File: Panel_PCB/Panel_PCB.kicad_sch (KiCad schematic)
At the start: 98 parts, among them J1 DC, J10 Relay 3, J11 Relay 4, J12 Terminal A, J13 Terminal B, J2 Bateria, J3 Sensor IN, J4 Sensor OUT, J5 Boton 1, J6 Boton 2, J7 Boton 3, J8 Relay 1, J9 Relay 2, K1 SANYOU_SRD_Form_C, K2 SANYOU_SRD_Form_C, K3 SANYOU_SRD_Form_C, K4 SANYOU_SRD_Form_C, K5 EC2-4.5SNU, K7 SANYOU_SRD_Form_C, Q1 2N2222A, Q2 2N2222A, Q3 2N2222A, Q4 2N2222A, Q7 2N2222A, U1 TLP291, U10 LM1117T-3.3, U11 LM7812_TO220, U12 DS1307+, U13 LM311, U2 TLP291, U3 TLP291, U4 TLP291, U5 LM7805_TO220, U6 LM1117T-3.3, U7 LM7805_TO220, U8 LM7805_TO220, U9 LM1117T-3.3, Y1 Crystal

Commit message: Actualización
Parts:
- removed C15: 0.1 μF, Capacitor_THT:C_Disc_D3.0mm_W1.6mm_P2.50mm, symbol Device:C_US
- removed C16: 0.22 μF, Capacitor_THT:C_Disc_D3.0mm_W1.6mm_P2.50mm, symbol Device:C_US
- removed D10, D11, D15, D17, D8: 1N4001, Diode_THT:D_DO-41_SOD81_P10.16mm_Horizontal, symbol Diode:1N4001
- removed R15, R16: 100 Ω 2W, Resistor_THT:R_Axial_DIN0617_L17.0mm_D6.0mm_P25.40mm_Horizontal, symbol Device:R_US
- removed R17: 1K, Resistor_THT:R_Axial_DIN0309_L9.0mm_D3.2mm_P12.70mm_Horizontal, symbol Device:R_US
- removed U11: LM7812_TO220, Package_TO_SOT_THT:TO-220-3_Vertical, symbol Regulator_Linear:LM7812_TO220
- added D19: 1N4001, Diode_THT:D_DO-41_SOD81_P10.16mm_Horizontal, symbol Diode:1N4001
- R2: value 100 Ω 2W -> 20 Ω 10W
- R21: value 220 -> 50
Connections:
- net at C1.2, C10.2, C11.2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: now also J1.1 (Pin_1), D19.2 (A)
- net at D16.1 (K), K7.5: now also D1.1 (K), K5.1, K5.4, D19.1 (K)
- net at J2.1 (Pin_1): now also D18.2 (A), K5.10, K7.3; no longer D7.2 (A)
- net at K5.5, R2.1: now also D7.1 (K); no longer K5.9
- net at D1.2 (A), F1.2: now also K7.1
- new net: D7.2 (A), K5.9
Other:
- note added: "El circuito puede funcionar a 10 VDC y 1 A debido a esto y por simplicidad, se decide cargar la bateria con 12 VDC"
- note removed: "Se necesitan al menos 14 VDC"
- moved on the sheet: D1, D7, K5

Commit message: Actualización
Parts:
- removed R2: 20 Ω 10W, Resistor_THT:R_Axial_DIN0617_L17.0mm_D6.0mm_P25.40mm_Horizontal, symbol Device:R_US
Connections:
- net at D7.1 (K), K5.5: now also C2.1, C7.1, C9.1, D2.1 (K), D3.1 (K), D4.1 (K), D5.1 (K), D6.1 (K), D9.2 (A), K1.5, K2.5, K3.5, K4.5, R10.1, R4.1, R6.1, R8.1, U7.1 (VI), U8.1 (VI)
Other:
- note added: "Con base en pruebas, aqui hay 11 VDC"
- note removed: "Debido a los diodos anteriores se debe virificar si hay 12V exactos"
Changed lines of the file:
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@@
 		)
 	)
-	(text "Debido a los diodos anteriores \nse debe virificar si hay 12V exactos"
+	(text "Con base en pruebas, aqui hay 11 VDC"
 		(exclude_from_sim no)
-		(at 309.626 236.982 0)
+		(at 309.88 244.602 0)
 		(effects
 			(font
@@
 	)
 	(junction
+		(at 300.99 247.65)
+		(diameter 0)
+		(color 0 0 0 0)
+	)
+	(junction
 		(at 482.6 73.66)
 		(diameter 0)
@@
 	)
 	(junction
-		(at 300.99 247.65)
-		(diameter 0)
-		(color 0 0 0 0)
-	)
-	(junction
 		(at 468.63 193.04)
 		(diameter 0)
@@
 	(wire
 		(pts
+			(xy 288.29 247.65) (xy 300.99 247.65)
+		)
+		(stroke
+			(width 0)
+			(type default)
+			(color 255 0 0 1)
+		)
+	)
+	(wire
+		(pts
 			(xy 224.79 182.88) (xy 224.79 200.66)
 		)
@@
 	(wire
 		(pts
-			(xy 288.29 247.65) (xy 292.1 247.65)
-		)
-		(stroke
-			(width 0)
-			(type default)
-			(color 255 0 0 1)
-		)
-	)
-	(wire
-		(pts
 			(xy 482.6 50.8) (xy 482.6 58.42)
 		)
@@
 	(wire
 		(pts
-			(xy 299.72 247.65) (xy 300.99 247.65)
-		)
-		(stroke
-			(width 0)
-			(type default)
-			(color 255 0 0 1)
-		)
-	)
-	(wire
-		(pts
 			(xy 203.2 194.31) (xy 203.2 204.47)
 		)
@@
 					(unit 1)
 				)
-			)
-		)
-	)
-	(symbol
-		(lib_id "Device:R_US")
-		(at 295.91 247.65 90)
-		(unit 1)
-		(exclude_from_sim no)
-		(in_bom yes)
-		(on_board yes)
-		(dnp no)
-		(fields_autoplaced yes)
-		(property "Reference" "R2"
-			(at 295.91 241.3 90)
-			(effects
-				(font
-					(size 1.27 1.27)
-				)
-			)
-		)
-		(property "Value" "20 Ω 10W"
-			(at 295.91 243.84 90)
-			(effects
-				(font
-					(size 1.27 1.27)
-				)
-			)
-		)
-		(property "Footprint" "Resistor_THT:R_Axial_DIN0617_L17.0mm_D6.0mm_P25.40mm_Horizontal"
-			(at 296.164 246.634 90)
-			(effects
-				(font
-					(size 1.27 1.27)
-				)
-				(hide yes)
-			)
-		)
-		(property "Datasheet" "~"
-			(at 295.91 247.65 0)
-			(effects
-				(font
-					(size 1.27 1.27)
-				)
-				(hide yes)
-			)
-		)
-		(property "Description" "Resistor, US symbol"
-			(at 295.91 247.65 0)
-			(effects
-				(font
-					(size 1.27 1.27)
-				)
-				(hide yes)
-			)
-		)
-		(pin "2"
-		)
-		(pin "1"
-		)
-		(instances
-			(project "Panel_PCB"
-				(path "/f7146f60-4eeb-4a38-9050-767b0cc7f13c"
-					(reference "R2")
-					(unit 1)
-				)

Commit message: Actualización
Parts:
- removed D9: 1N4001, Diode_THT:D_DO-41_SOD81_P10.16mm_Horizontal, symbol Diode:1N4001
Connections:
- net at D12.2 (A): now also C2.1, C7.1, C9.1, D2.1 (K), D3.1 (K), D4.1 (K), D5.1 (K), D6.1 (K), D7.1 (K), K1.5, K2.5, K3.5, K4.5, K5.5, R10.1, R4.1, R6.1, R8.1, U7.1 (VI), U8.1 (VI)
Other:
- note added: "AUX"
- note added: "Puerta"
- note removed: "Puerta 1"
- note removed: "Puerta 2"
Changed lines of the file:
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@@
 		)
 	)
-	(text "Puerta 2"
+	(text "Luz emergencia"
 		(exclude_from_sim no)
 		(at 488.95 483.362 0)
@@
 		)
 	)
-	(text "Puerta 1"
+	(text "Puerta"
 		(exclude_from_sim no)
 		(at 416.306 484.124 0)
@@
 		)
 	)
-	(text "Luz emergencia"
+	(text "Señal panico"
 		(exclude_from_sim no)
 		(at 560.578 483.108 0)
@@
 		)
 	)
-	(text "Señal panico"
+	(text "AUX\n"
 		(exclude_from_sim no)
 		(at 634.746 482.854 0)
@@
 	(wire
 		(pts
+			(xy 356.87 53.34) (xy 356.87 247.65)
+		)
+		(stroke
+			(width 0)
+			(type default)
+			(color 255 0 0 1)
+		)
+	)
+	(wire
+		(pts
 			(xy 542.29 339.09) (xy 471.17 339.09)
 		)
@@
 	(wire
 		(pts
-			(xy 356.87 53.34) (xy 356.87 54.61)
-		)
-		(stroke
-			(width 0)
-			(type default)
-		)
-	)
-	(wire
-		(pts
 			(xy 469.9 215.9) (xy 565.15 215.9)
 		)
@@
 	(wire
 		(pts
-			(xy 356.87 62.23) (xy 356.87 247.65)
-		)
-		(stroke
-			(width 0)
-			(type default)
-			(color 255 0 0 1)
-		)
-	)
-	(wire
-		(pts
 			(xy 148.59 247.65) (xy 154.94 247.65)
 		)
@@
 					(unit 1)
 				)
-			)
-		)
-	)
-	(symbol
-		(lib_id "Diode:1N4001")
-		(at 356.87 58.42 270)
-		(unit 1)
-		(exclude_from_sim no)
-		(in_bom yes)
-		(on_board yes)
-		(dnp no)
-		(property "Reference" "D9"
-			(at 360.426 57.404 0)
-			(effects
-				(font
-					(size 1.27 1.27)
-				)
-				(justify left)
-			)
-		)
-		(property "Value" "1N4001"
-			(at 362.712 55.118 0)
-			(effects
-				(font
-					(size 1.27 1.27)
-				)
-				(justify left)
-			)
-		)
-		(property "Footprint" "Diode_THT:D_DO-41_SOD81_P10.16mm_Horizontal"
-			(at 356.87 58.42 0)
-			(effects
-				(font
-					(size 1.27 1.27)
-				)
-				(hide yes)
-			)
-		)
-		(property "Datasheet" "http://www.vishay.com/docs/88503/1n4001.pdf"
-			(at 356.87 58.42 0)
-			(effects
-				(font
-					(size 1.27 1.27)
-				)
-				(hide yes)
-			)
-		)
-		(property "Description" "50V 1A General Purpose Rectifier Diode, DO-41"
-			(at 356.87 58.42 0)
-			(effects
-				(font
-					(size 1.27 1.27)
-				)
-				(hide yes)
-			)
-		)
-		(property "Sim.Device" "D"
-			(at 356.87 58.42 0)
-			(effects
-				(font
-					(size 1.27 1.27)
-				)
-				(hide yes)
-			)
-		)
-		(property "Sim.Pins" "1=K 2=A"
-			(at 356.87 58.42 0)
-			(effects
-				(font
-					(size 1.27 1.27)
-				)
-				(hide yes)
-			)
-		)
-		(pin "1"
-		)
-		(pin "2"
-		)
-		(instances
-			(project "Panel_PCB"
-				(path "/f7146f60-4eeb-4a38-9050-767b0cc7f13c"
-					(reference "D9")
-					(unit 1)
-				)

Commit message: Actualización del esquema y el software
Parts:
- added J14: Boton D (4), TerminalBlock_Phoenix:TerminalBlock_Phoenix_MKDS-1,5-2-5.08_1x02_P5.08mm_Horizontal, symbol Connector:Screw_Terminal_01x02
- J5: value Boton 1 -> Boton A (1)
- J6: value Boton 2 -> Boton B (2)
- J7: value Boton 3 -> Boton C (3)
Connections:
- net at C1.2, C10.2, C11.2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: now also J14.1 (Pin_1)
- net at J13.13 (Pin_13): now also J14.2 (Pin_2)
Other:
- note added: "Boton A (1)"
- note added: "Boton B (2)"
- note added: "Boton C (3)"
- note added: "Boton D (4)"
- note removed: "Boton 1"
- note removed: "Boton 2"
- note removed: "Boton 3"
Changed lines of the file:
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@@
 		)
 	)
-	(text "Boton 1"
+	(text "Boton A (1)"
 		(exclude_from_sim no)
-		(at 596.138 178.562 0)
+		(at 601.726 178.562 0)
 		(effects
 			(font
@@
 		)
 	)
-	(text "Boton 2"
+	(text "Boton B (2)"
 		(exclude_from_sim no)
 		(at 596.392 202.946 0)
@@
 		)
 	)
-	(text "Boton 3"
+	(text "Boton C (3)"
 		(exclude_from_sim no)
 		(at 595.122 227.33 0)
@@
 		)
 	)
+	(text "Boton D (4)"
+		(exclude_from_sim no)
+		(at 591.82 250.444 0)
+		(effects
+			(font
+				(size 1.27 1.27)
+			)
+		)
+	)
 	(text "Sensor salida"
 		(exclude_from_sim no)
@@
 	)
 	(junction
-		(at 535.94 129.54)
-		(diameter 0)
-		(color 0 0 0 0)
-	)
-	(junction
 		(at 411.48 154.94)
 		(diameter 0)
@@
 	)
 	(junction
+		(at 528.32 193.04)
+		(diameter 0)
+		(color 0 0 0 0)
+	)
+	(junction
 		(at 308.61 267.97)
 		(diameter 0)
@@
 	)
 	(junction
+		(at 478.79 129.54)
+		(diameter 0)
+		(color 0 0 0 0)
+	)
+	(junction
 		(at 433.07 193.04)
 		(diameter 0)
@@
 	)
 	(junction
+		(at 478.79 154.94)
+		(diameter 0)
+		(color 0 0 0 0)
+	)
+	(junction
 		(at 687.07 311.15)
 		(diameter 0)
@@
 	)
 	(junction
-		(at 535.94 154.94)
-		(diameter 0)
-		(color 0 0 0 0)
-	)
-	(junction
 		(at 468.63 177.8)
 		(diameter 0)
@@
 	(wire
 		(pts
+			(xy 478.79 129.54) (xy 613.41 129.54)
+		)
+		(stroke
+			(width 0)
+			(type default)
+		)
+	)
+	(wire
+		(pts
 			(xy 154.94 167.64) (xy 154.94 247.65)
 		)
@@
 	(wire
 		(pts
-			(xy 435.61 154.94) (xy 535.94 154.94)
+			(xy 435.61 154.94) (xy 478.79 154.94)
 		)
 		(stroke
@@
 	(wire
 		(pts
+			(xy 548.64 193.04) (xy 528.32 193.04)
+		)
+		(stroke
+			(width 0)
+			(type default)
+			(color 0 0 0 1)
+		)
+	)
+	(wire
+		(pts
 			(xy 542.29 265.43) (xy 698.5 265.43)
 		)
@@
 	(wire
 		(pts
+			(xy 478.79 154.94) (xy 610.87 154.94)
+		)
+		(stroke
+			(width 0)
+			(type default)
+		)
+	)
+	(wire
+		(pts
 			(xy 441.96 189.23) (xy 441.96 193.04)
 		)
@@
 	(wire
 		(pts
+			(xy 596.9 270.51) (xy 532.13 270.51)
+		)
+		(stroke
+			(width 0)
+			(type default)
+		)
+	)
+	(wire
+		(pts
 			(xy 534.67 408.94) (xy 537.21 408.94)
 		)
@@
 	(wire
 		(pts
-			(xy 414.02 129.54) (xy 535.94 129.54)
+			(xy 414.02 129.54) (xy 478.79 129.54)
 		)
 		(stroke
@@
 	(wire
 		(pts
-			(xy 468.63 177.8) (xy 535.94 177.8)
+			(xy 468.63 177.8) (xy 478.79 177.8)
 		)
 		(stroke
@@
 	(wire
 		(pts
+			(xy 551.18 252.73) (xy 596.9 252.73)
+		)
+		(stroke
+			(width 0)
+			(type default)
+		)
+	)
+	(wire
+		(pts
 			(xy 382.27 215.9) (xy 396.24 215.9)
 		)
@@
 	(wire
 		(pts
+			(xy 551.18 107.95) (xy 551.18 252.73)
+		)
+		(stroke
+			(width 0)
+			(type default)
+		)
+	)
+	(wire
+		(pts
 			(xy 308.61 247.65) (xy 308.61 255.27)
 		)
@@
 	(wire
 		(pts
-			(xy 535.94 129.54) (xy 613.41 129.54)
-		)
-		(stroke
-			(width 0)
-			(type default)
-		)
-	)
-	(wire
-		(pts
 			(xy 608.33 408.94) (xy 610.87 408.94)
 		)
@@
 	(wire
 		(pts
-			(xy 535.94 154.94) (xy 535.94 129.54)
+			(xy 478.79 154.94) (xy 478.79 129.54)
 		)
 		(stroke
@@
 	(wire
 		(pts
-			(xy 535.94 154.94) (xy 610.87 154.94)
-		)
-		(stroke
-			(width 0)
-			(type default)
-		)
-	)
-	(wire
-		(pts
 			(xy 547.37 285.75) (xy 547.37 344.17)
 		)
@@
 	(wire
 		(pts
+			(xy 596.9 252.73) (xy 596.9 270.51)
+		)
+		(stroke
+			(width 0)
+			(type default)
+		)
+	)
+	(wire
+		(pts
 			(xy 615.95 339.09) (xy 615.95 367.03)
 		)
@@
 	(wire
 		(pts
-			(xy 535.94 177.8) (xy 535.94 154.94)
+			(xy 548.64 107.95) (xy 548.64 193.04)
+		)
+		(stroke
+			(width 0)
+			(type default)
+			(color 0 0 0 1)
+		)
+	)
+	(wire
+		(pts
+			(xy 478.79 177.8) (xy 478.79 154.94)
 		)
 		(stroke
@@
 	)
 	(symbol
+		(lib_id "Connector:Screw_Terminal_01x02")
+		(at 548.64 102.87 90)
+		(unit 1)
+		(exclude_from_sim no)
+		(in_bom yes)
+		(on_board yes)
+		(dnp no)
+		(property "Reference" "J14"
+			(at 547.624 97.028 90)
+			(effects
+				(font
+					(size 1.27 1.27)
+				)
+				(justify right)
+			)
+		)
+		(property "Value" "Boton D (4)"
+			(at 544.068 99.314 90)
+			(effects
+				(font
+					(size 1.27 1.27)
+				)
+				(justify right)
+			)
+		)
+		(property "Footprint" "TerminalBlock_Phoenix:TerminalBlock_Phoenix_MKDS-1,5-2-5.08_1x02_P5.08mm_Horizontal"
+			(at 548.64 102.87 0)
+			(effects
+				(font
+					(size 1.27 1.27)
+				)
+				(hide yes)
+			)
+		)
+		(property "Datasheet" "~"
+			(at 548.64 102.87 0)
+			(effects
+				(font
+					(size 1.27 1.27)
+				)
+				(hide yes)
+			)
+		)
+		(property "Description" "Generic screw terminal, single row, 01x02, script generated (kicad-library-utils/schlib/autogen/connector/)"
+			(at 548.64 102.87 0)
+			(effects
+				(font
+					(size 1.27 1.27)
+				)
+				(hide yes)
+			)
+		)
+		(pin "2"
+		)
+		(pin "1"
+		)
+		(instances
+			(project "Panel_PCB"
+				(path "/f7146f60-4eeb-4a38-9050-767b0cc7f13c"
+					(reference "J14")
+					(unit 1)
+				)
+			)
+		)
+	)
+	(symbol
 		(lib_id "Device:C_US")
 		(at 468.63 185.42 0)
@@
 		(dnp no)
 		(property "Reference" "J6"
-			(at 496.316 101.854 90)
+			(at 505.968 97.028 90)
 			(effects
 				(font
@@
 			)
 		)
-		(property "Value" "Boton 2"
-			(at 496.316 104.394 90)
+		(property "Value" "Boton B (2)"
+			(at 502.158 99.314 90)
 			(effects
 				(font
@@
 		(dnp no)
 		(property "Reference" "J7"
-			(at 517.906 101.854 90)
+			(at 528.574 96.774 90)
 			(effects
 				(font
@@
 			)
 		)
-		(property "Value" "Boton 3"
-			(at 517.906 104.394 90)
+		(property "Value" "Boton C (3)"
+			(at 524.51 99.314 90)
 			(effects
 				(font
@@
 		(dnp no)
 		(property "Reference" "J5"
-			(at 473.456 101.854 90)
+			(at 483.616 97.028 90)
 			(effects
 				(font
@@
 			)
 		)
-		(property "Value" "Boton 1"
-			(at 473.456 104.394 90)
+		(property "Value" "Boton A (1)"
+			(at 480.06 99.568 90)
 			(effects
 				(font

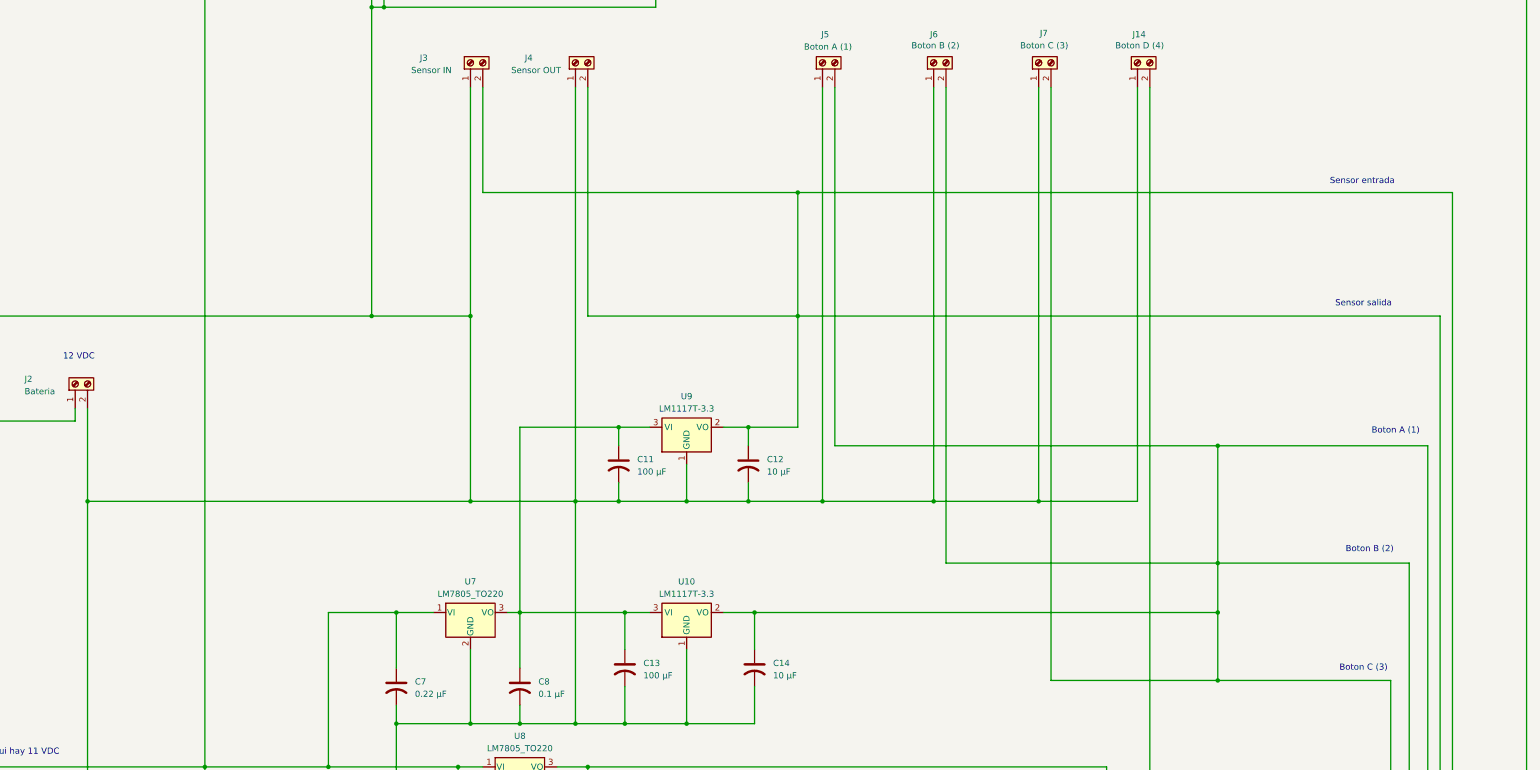
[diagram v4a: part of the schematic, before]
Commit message: Corrección a las entradas
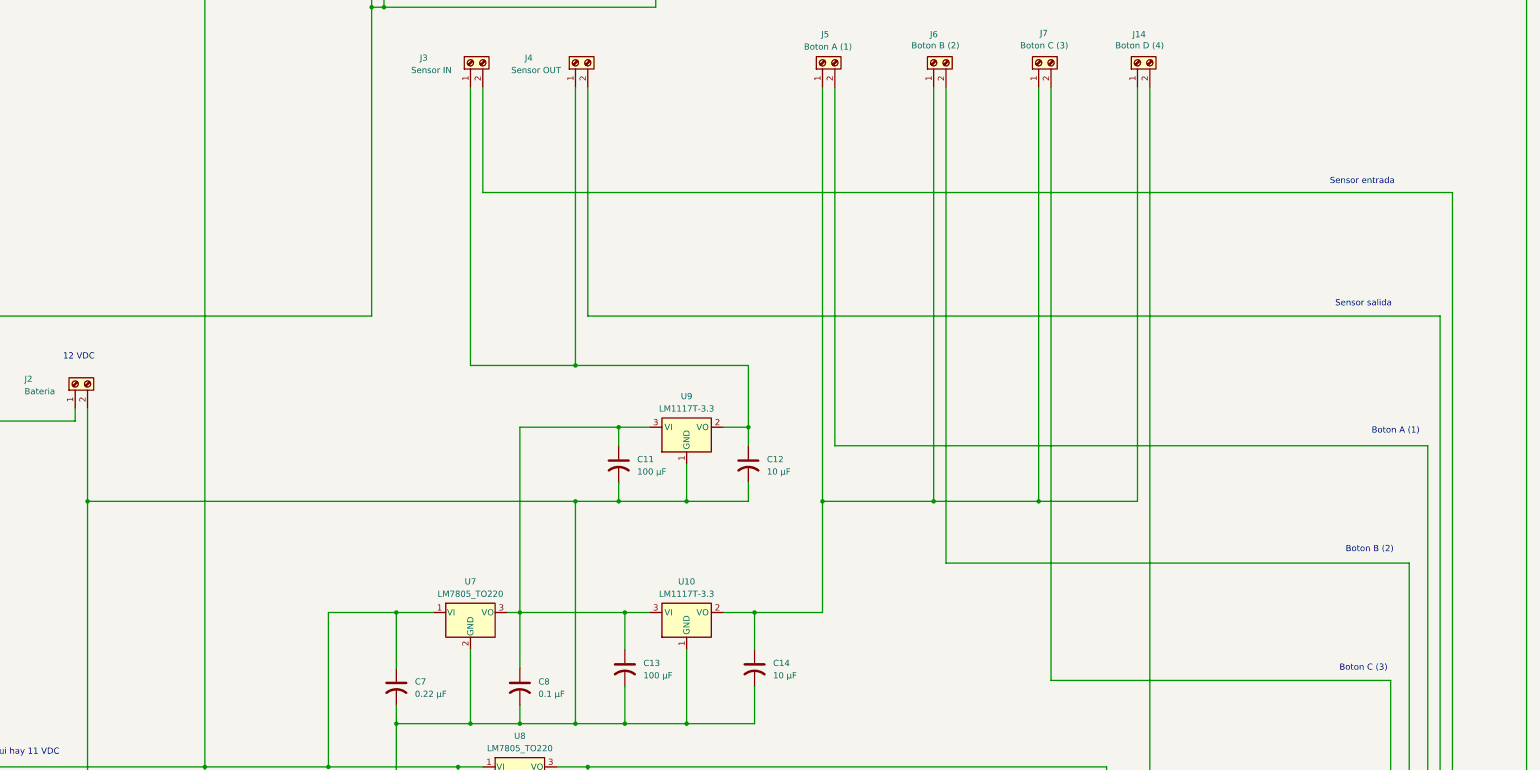
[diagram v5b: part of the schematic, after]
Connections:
- net at C10.2, C11.2, C12.2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: no longer C1.2, C3.2, J14.1 (Pin_1), J3.1 (Pin_1), J4.1 (Pin_1), J5.1 (Pin_1), J6.1 (Pin_1), J7.1 (Pin_1), R21.2, R26.2, U13.4 (V-), U5.2 (GND), U6.1 (GND)
- new net: C14.1, J14.1 (Pin_1), J5.1 (Pin_1), J6.1 (Pin_1), J7.1 (Pin_1), U10.2 (VO)
- new net: C12.1, J3.1 (Pin_1), J4.1 (Pin_1), U9.2 (VO)
- new net: C1.2, C3.2, R21.2, R26.2, U13.4 (V-), U5.2 (GND), U6.1 (GND)
- new net: J13.10 (Pin_10), J6.2 (Pin_2)
- new net: J13.11 (Pin_11), J7.2 (Pin_2)
- new net: J13.4 (Pin_4), J3.2 (Pin_2)
- new net: J13.5 (Pin_5), J4.2 (Pin_2)
- new net: J13.9 (Pin_9), J5.2 (Pin_2)
